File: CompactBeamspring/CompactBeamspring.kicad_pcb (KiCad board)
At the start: 2 copper layers, 162.2 x 18.8 mm, 27 parts, among them J1 BEAMSPRING CONNECTOR, J3 EXPANSION HEADER, U1 MCP4921-E, U2 LM339A, U3 74AHC595, U4 74AHC595, U5 ProMicro, U7 74AHC595

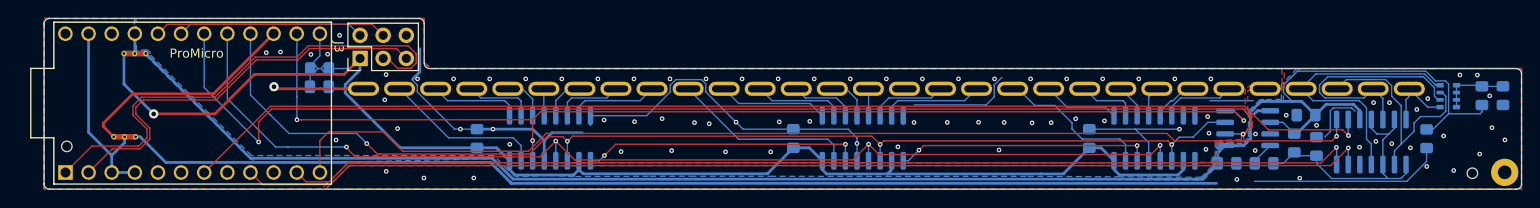
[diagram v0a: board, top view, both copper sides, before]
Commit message: made it th xwhatsit software compatible, added dac testpoints, added reset shorting pads, generally reworked to be nicer
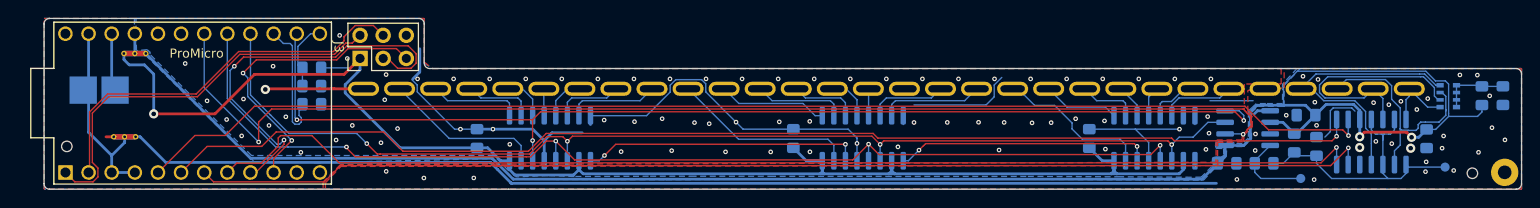
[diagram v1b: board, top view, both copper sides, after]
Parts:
- added J2: PadsToShort, TH-XWhatsIt:PadsToShort, B.Cu at (99.5, 147.0)
- added R8: Not Mounted, Resistor_SMD:R_0805_2012Metric_Pad1.15x1.40mm_HandSolder, B.Cu at (122.9, 151.4)
- added TP1: Dac Output, TestPoint:TestPoint_Pad_D1.0mm, B.Cu at (231.5, 159.6)
- added TP2: Threshold Voltage, TestPoint:TestPoint_Pad_D1.0mm, B.Cu at (247.3, 158.3)
- R6: value Not Mounted, Shorted -> Not Mounted; footprint TH-XWhatsIt:SHORTEDR_0805_2012Metric_Pad1.15x1.40mm_HandSolder -> Resistor_SMD:R_0805_2012Metric_Pad1.15x1.40mm_HandSolder
- moved R6 0.85 mm to (122.9, 147.4)
- moved R7 0.83 mm to (122.9, 149.4)
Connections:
- net Net-(NT1-Pad2) renamed GND
- U5 pad 1: HEADER1 -> HEADER3
- U5 pad 10: ROW6 -> HEADER2
- U5 pad 11: ROW3 -> Net-(U5-Pad11)
- U5 pad 12: ROW1 -> Net-(U5-Pad12)
- U5 pad 15: GNDD -> Net-(R8-Pad1)
- U5 pad 19: HEADER3 -> Net-(U5-Pad19)
- U5 pad 2: HEADER2 -> HEADER4
- U5 pad 20: HEADER4 -> Net-(U5-Pad20)
- U5 pad 5: ROW8 -> ROW2
- U5 pad 6: ROW7 -> ROW1
- U5 pad 7: ROW2 -> ROW4
- U5 pad 8: ROW5 -> ROW3
- U5 pad 9: ROW4 -> HEADER1
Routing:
- net HEADER3: track 20.6 -> 45.0 mm
- net GNDD: track 134.0 -> 110.9 mm, vias 63 -> 73
- net GNDA: track 152.6 -> 131.3 mm, vias 26 -> 32
- net HEADER4: track 25.7 -> 43.6 mm
- net Net-(R8-Pad1): track 0.00 -> 15.1 mm
- net ROW1: track 119.6 -> 132.8 mm
- net HEADER2: track 45.2 -> 33.4 mm, vias 0 -> 2
- net +5VD: track 148.1 -> 158.6 mm
- net HEADER1: track 54.2 -> 43.9 mm, vias 0 -> 2
- net +5VA: track 186.8 -> 196.9 mm, vias 0 -> 2
- net ROW3: track 118.2 -> 127.8 mm
- net RST: track 0.00 -> 6.35 mm
- net Net-(R4-Pad2): track 2.66 -> 8.98 mm
- net SETPOINT: track 28.3 -> 33.5 mm
- net ROW2: track 131.8 -> 136.9 mm
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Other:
- board text added: "DAC"
- board text added: "Threshold"
- board text added: "Voltage"
- board text added: "Vout"

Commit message: More mods
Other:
- board text added: "Compact-Beamspring Rev1.2"
- board text removed: "Compact-Beamspring Rev1.1"
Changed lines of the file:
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@@
   )
   (setup
-    (last_trace_width 0.3048)
+    (last_trace_width 0.1524)
     (user_trace_width 0.1524)
     (user_trace_width 0.3048)
@@
       (effects (font (size 1 1) (thickness 0.15)) (justify mirror))
     )
-    (fp_text user %R (at 0 1.45) (layer B.Fab)
-      (effects (font (size 1 1) (thickness 0.15)) (justify mirror))
-    )
     (fp_circle (center 0 0) (end 1 0) (layer B.CrtYd) (width 0.05))
     (fp_circle (center 0 0) (end 0 -0.7) (layer B.SilkS) (width 0.12))
+    (fp_text user %R (at 0 1.45) (layer B.Fab)
+      (effects (font (size 1 1) (thickness 0.15)) (justify mirror))
+    )
     (pad 1 smd circle (at 0 0) (size 1 1) (layers B.Cu B.Mask)
       (net 28 SETPOINT))
@@
       (effects (font (size 1 1) (thickness 0.15)) (justify mirror))
     )
-    (fp_text user %R (at 0 1.45) (layer B.Fab)
-      (effects (font (size 1 1) (thickness 0.15)) (justify mirror))
-    )
     (fp_circle (center 0 0) (end 1 0) (layer B.CrtYd) (width 0.05))
     (fp_circle (center 0 0) (end 0 -0.7) (layer B.SilkS) (width 0.12))
+    (fp_text user %R (at 0 1.45) (layer B.Fab)
+      (effects (font (size 1 1) (thickness 0.15)) (justify mirror))
+    )
     (pad 1 smd circle (at 0 0) (size 1 1) (layers B.Cu B.Mask)
       (net 29 "Net-(R4-Pad2)"))
@@
     (tags "resistor handsolder")
     (attr virtual)
-    (fp_text reference R8 (at -3.1 0.05) (layer B.SilkS)
+    (fp_text reference R8 (at -3.1 0.05 unlocked) (layer B.SilkS)
       (effects (font (size 1 1) (thickness 0.15)) (justify mirror))
     )
@@
     (tags "resistor handsolder")
     (attr virtual)
-    (fp_text reference R6 (at 3.1 -0.05) (layer B.SilkS)
+    (fp_text reference R6 (at 3.1 -0.05 unlocked) (layer B.SilkS)
       (effects (font (size 1 1) (thickness 0.15)) (justify mirror))
     )
@@
     (effects (font (size 1 1) (thickness 0.15)) (justify mirror))
   )
-  (gr_text "Compact-Beamspring\nRev1.1" (at 198 156.25) (layer B.SilkS)
+  (gr_text "Compact-Beamspring\nRev1.2" (at 198 156.25) (layer B.SilkS)
     (effects (font (size 1 1) (thickness 0.15)) (justify mirror))
   )
@@
   (segment (start 117.87462 149.72538) (end 117.8 149.8) (width 0.3048) (layer F.Cu) (net 52))
   (segment (start 123.78944 149.72538) (end 117.87462 149.72538) (width 0.3048) (layer F.Cu) (net 52))
-  (segment (start 103.4669 158.91662) (end 100.9269 158.91662) (width 0.3048) (layer B.Cu) (net 61))
-  (segment (start 100.9269 158.91662) (end 100.9269 157.04718) (width 0.3048) (layer B.Cu) (net 61))
-  (segment (start 100.9269 157.04718) (end 98.3869 154.50718) (width 0.3048) (layer B.Cu) (net 61))
-  (segment (start 102.35184 155.62224) (end 100.9269 157.04718) (width 0.3048) (layer B.Cu) (net 61))
-  (segment (start 102.35184 154.9974) (end 102.35184 155.62224) (width 0.3048) (layer B.Cu) (net 61))
   (segment (start 103.47198 143.6817) (end 103.4669 143.67662) (width 0.3048) (layer B.Cu) (net 53))
   (segment (start 103.47198 145.8534) (end 103.47198 143.6817) (width 0.3048) (layer B.Cu) (net 53))
@@
   (segment (start 121.501409 151.798591) (end 121.875 151.425) (width 0.1524) (layer B.Cu) (net 56))
   (segment (start 121.501409 152.648919) (end 121.501409 151.798591) (width 0.1524) (layer B.Cu) (net 56))
+  (segment (start 103.4669 158.91662) (end 100.9269 158.91662) (width 0.3048) (layer B.Cu) (net 61))
+  (segment (start 100.9269 158.91662) (end 100.9269 157.04718) (width 0.3048) (layer B.Cu) (net 61))
+  (segment (start 100.9269 157.04718) (end 98.3869 154.50718) (width 0.3048) (layer B.Cu) (net 61))
+  (segment (start 102.35184 155.62224) (end 100.9269 157.04718) (width 0.3048) (layer B.Cu) (net 61))
+  (segment (start 102.35184 154.9974) (end 102.35184 155.62224) (width 0.3048) (layer B.Cu) (net 61))
   (segment (start 98.15 149.875) (end 98.3869 149.6381) (width 0.3048) (layer B.Cu) (net 61))
   (segment (start 97.8 149.875) (end 98.15 149.875) (width 0.3048) (layer B.Cu) (net 61))

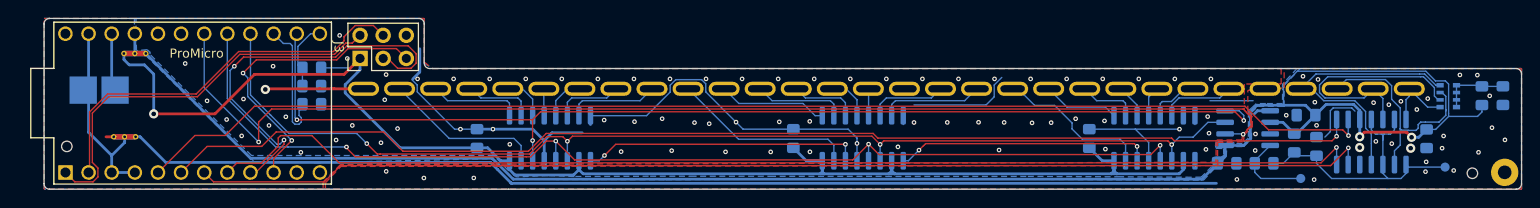
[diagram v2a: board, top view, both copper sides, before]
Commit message: Moved to individual resistors instead of resistor network, added a bit more space next to the promicro
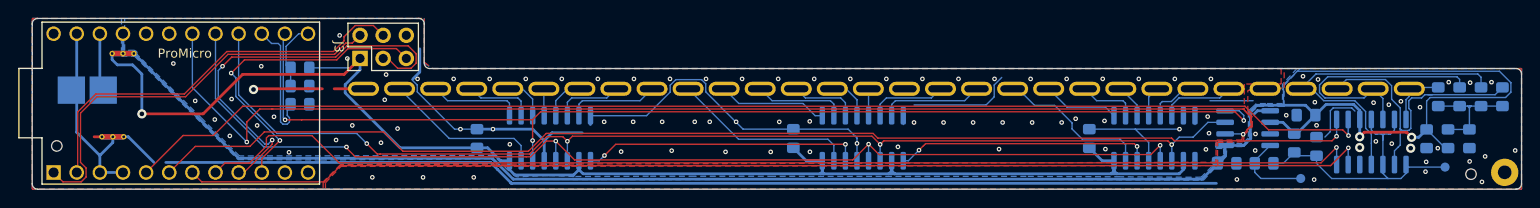
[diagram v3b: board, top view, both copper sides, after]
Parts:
- removed the REF** at (96.0, 156.1)
- removed the REF** at (250.3, 159.0)
- removed RN1: 100K, Resistor_SMD:R_Array_Convex_4x0603
- added R10: 100k 1%, Resistor_SMD:R_0805_2012Metric_Pad1.15x1.40mm_HandSolder, B.Cu at (246.6, 150.6)
- added R11: 100k 1%, Resistor_SMD:R_0805_2012Metric_Pad1.15x1.40mm_HandSolder, B.Cu at (251.3, 150.6)
- added R12: 100k 1%, Resistor_SMD:R_0805_2012Metric_Pad1.15x1.40mm_HandSolder, B.Cu at (253.7, 150.6)
- added R9: 100k 1%, Resistor_SMD:R_0805_2012Metric_Pad1.15x1.40mm_HandSolder, B.Cu at (248.9, 150.6)
- added REF**: tooling_hole, TH-XWhatsIt:tooling_hole, F.Cu at (94.9, 156.0)
- added REF**: tooling_hole, TH-XWhatsIt:tooling_hole, F.Cu at (250.2, 159.1)
- moved R1 6.02 mm to (247.7, 155.2)
- moved R2 6.00 mm to (250.0, 155.2)
- moved NT1 1.30 mm to (99.9, 155.0)
- moved R6 1.30 mm to (121.6, 147.4)
- moved R7 1.30 mm to (121.6, 149.4)
- moved R8 1.30 mm to (121.6, 151.4)
- moved J2 1.30 mm to (98.2, 147.0)
- moved NT2 1.30 mm to (101.0, 145.9)
- moved U5 1.30 mm to (108.5, 151.3)
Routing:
- net +5VA: track 196.9 -> 210.6 mm
- net SENSE3: track 26.0 -> 32.1 mm
- net SENSE4: track 30.6 -> 35.9 mm
- net BIAS: track 7.55 -> 12.5 mm
- net +5VD: track 158.6 -> 161.2 mm
- net SENSE2: track 26.4 -> 28.0 mm
- net ~SELECTDAC: track 130.8 -> 132.2 mm
- net MOSI: track 122.7 -> 124.0 mm
- net HEADER2: track 33.4 -> 34.7 mm
- net ROW1: track 132.8 -> 134.1 mm
- net LOADCOL: track 121.2 -> 122.5 mm
- net ROW3: track 127.8 -> 129.1 mm
- net HEADER1: track 43.9 -> 45.2 mm
- net HEADER4: track 43.6 -> 44.9 mm
- net HEADER3: track 45.0 -> 46.3 mm
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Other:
- board size 162.2 x 18.8 mm -> 163.6 x 18.8 mm
- board text added: "Compact-Beamspring Rev1.3"
- board text removed: "Compact-Beamspring Rev1.2"

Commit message: Updated Pro Micro and solenoid header footprint for more correct rendering
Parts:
- J1: footprint TH-XWhatsIt:30-pin-universal-beamspring-connector_v2 -> TH-XWhatsIt:30-pin-universal-beamspring-connector_v3_onlyflat
